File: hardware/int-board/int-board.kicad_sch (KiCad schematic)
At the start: 34 parts, among them J1 PTSM 0,5/4-HH, J2 PTSM 0,5/4-HH, J3 PTSM 0,5/4-HH, J4 PTSM 0,5/4-HH, J5 Pi 40-pin socket, J6 LINK to EXT, J7 PWR link (not fitted), J8 spare ch pads, J9 breakout, U1 LTV-847, U2 LTV-847, U3 LTV-847

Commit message: hardware: INT link headers move into the housing's right-hand slot; review checklist in docs
The enclosure leaves no clearance around the board except the opening for
the four top-edge plugs and a slot on the right-hand side, rows 9-23, the
height of a PTSM socket (David, 2026-09-12). J6 and J7 sit in that slot
with their entries facing the edge, pin row 6.3 mm inside it so the pads
clear the rib's bulges at x 49.8; the MOV position, test points and J8
move to the bottom-left field the links vacated. Header pin 1 stays open
on the board like the spare grounds: the column blocks a track from pin 1
to pin 17, and the router otherwise reached the link from pin 1 and left
17's breakout stranded. A via keepout ring 0.8 mm inside the outline stops
the router placing vias against the 0.3 mm edge rule, which the DSN does
not carry. gen-boards.py also gains the GND_BUS_X import it lost when the
constants moved to gen_tables.py.

Routed, DRC clean, schematic parity kept; Gerbers re-exported. The
"before you order" checklist is docs/rpi-io-boards-review.md.

Co-Authored-By: Claude Fable 5.1 <noreply@anthropic.com>
Claude-Session: https://claude.ai/code/session_01WPMStupqhasFMcGr3goMno
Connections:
- net 3V3: no longer J5.1 (Pin_1)
- no-connect marks 11 -> 12

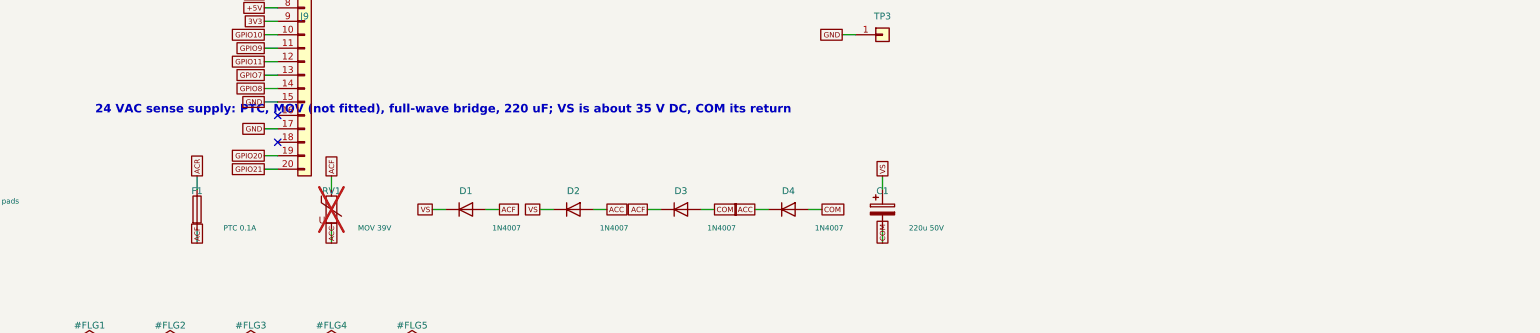
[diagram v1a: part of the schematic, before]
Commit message: hardware: every INT component-side part held to the DIP-socket height; the Pi mapped under the board
The cover's inner depth is unmeasured, but the built board proves it clears
a DIP socket with its chip, about 8 mm, so no fitted part may stand taller.
The 12.5 mm radial capacitor becomes a 100 uF 63 V axial lying flat along
the bottom-left field (6.5 x 18, 6.9 mm); 100 uF holds the 35 V rail's
ripple to 2.8 V at 34 mA and the value is not critical. The PTC disc and the
MOV position lie flat on new pivac footprints. The test points, spare pads
and proto field move to suit.

Appendix A.3 of the plan maps the Pi 4B's connectors onto the INT board
from the RP-008343 mechanical drawing, with the room each leaves on the
solder side at the 16 mm socket stack: none under the USB stacks, where
every joint is trimmed flush, as the built board already requires.

Routed, DRC clean, schematic parity kept; Gerbers re-exported.

Co-Authored-By: Claude Fable 5.1 <noreply@anthropic.com>
Claude-Session: https://claude.ai/code/session_01WPMStupqhasFMcGr3goMno
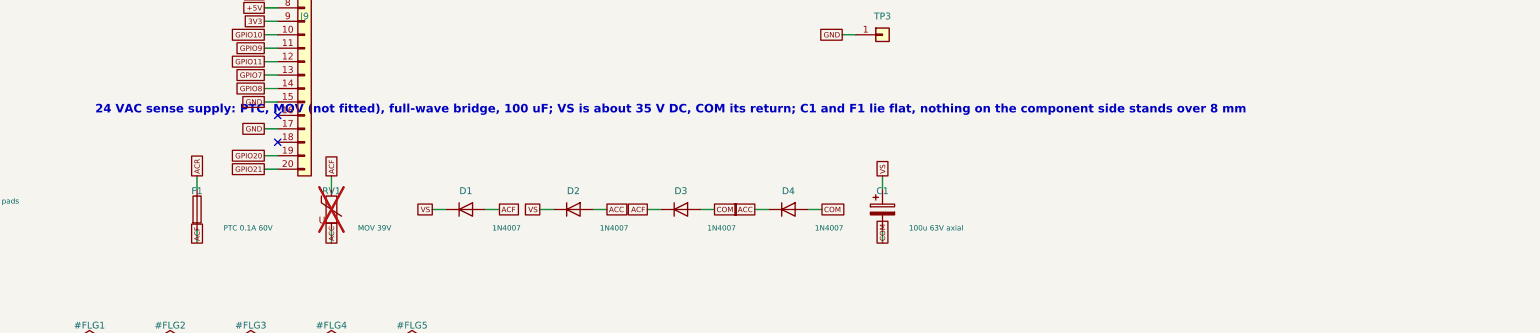
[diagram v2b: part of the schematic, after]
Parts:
- C1: value 220u 50V -> 100u 63V axial; footprint Capacitor_THT:CP_Radial_D10.0mm_P5.00mm -> Capacitor_THT:CP_Axial_L18.0mm_D6.5mm_P25.00mm_Horizontal
- F1: value PTC 0.1A -> PTC 0.1A 60V; footprint pivac:PTC_Radial_P5.08 -> pivac:PTC_Radial_P5.08_Flat
- RV1: footprint pivac:MOV_Radial_P5.0 -> pivac:MOV_Radial_P5.0_Flat
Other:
- note added: "24 VAC sense supply: PTC, MOV (not fitted), full-wave bridge, 100 uF; VS is about 35 V DC, COM its return; C1 and F1 lie flat, nothing on the component side stands over 8 mm"
- note removed: "24 VAC sense supply: PTC, MOV (not fitted), full-wave bridge, 220 uF; VS is about 35 V DC, COM its return"

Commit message: hardware: no through-hole part over the Pi's USB stacks; the capacitor stands between J4 and J6
The USB shells are Pi ground and the rectifier's nets are 35 V above COM,
so a pin tail under a USB stack, where the 16 mm socket stack leaves no
room, is a short waiting to happen (David, 2026-09-12). The bottom-left
field now carries nothing: the capacitor stands between J4 and the link
slot, right of the resistor columns (pitch 3.3 mm) and left of the housing
rib, with the PTC and the MOV position lying flat beside it; the four
diodes form one column at the bottom right past the USB stacks, with the
test points and the spare-channel pads (now a row) below them; the
prototyping field is gone. The link headers' pin row moves to 6.0 mm inside
the edge so their courtyards clear the capacitor's.

docs/rpi-io-boards-review.md and the review page gain a table of what
every reference designator on each board is for.

Routed, DRC clean, schematic parity kept; Gerbers re-exported.

Co-Authored-By: Claude Fable 5.1 <noreply@anthropic.com>
Claude-Session: https://claude.ai/code/session_01WPMStupqhasFMcGr3goMno
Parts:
- J8: footprint pivac:Pads_1x3 -> pivac:Pads_3x1

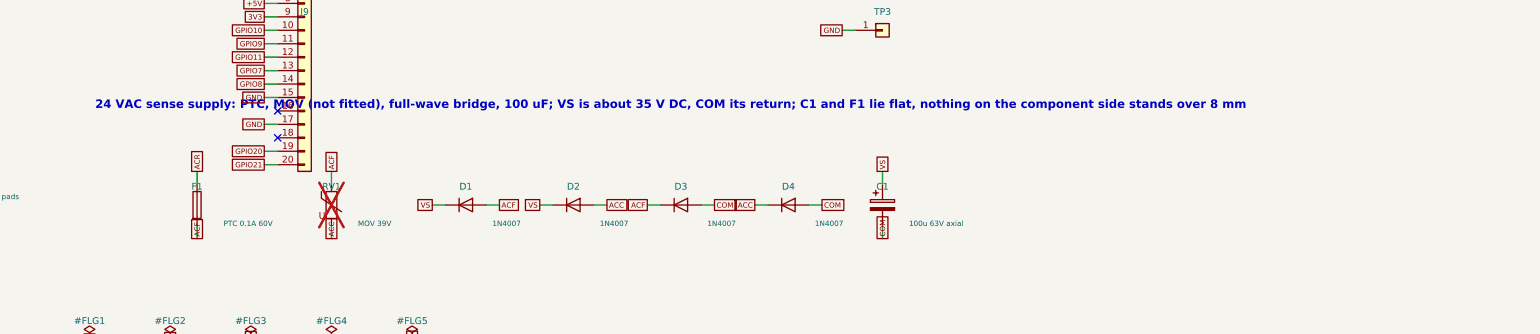
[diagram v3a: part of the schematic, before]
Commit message: hardware: silkscreen tidied, MOV position dropped, copper plots for the review
Plug designators sit below their pin labels (J4's beside the capacitor),
the resistor references run along their bodies, the diode references sit
at the board edge end of each diode, the link header references sit on the
rib strip beside them, the capacitor's beside its lower pad, and the empty
bottom field says why it is empty. The MOV position is gone: the strip
beside the capacitor holds the PTC and the J4 labels, and a clamp on a
class 2 transformer's 24 VAC is a nicety. GPIO8's run from header pin 24
to its breakout pad, which threads the column twice through 0.84 mm gaps,
is laid by hand because the router managed it only sometimes. EXT: C1's
reference moves below the part, clear of the H2 label.

Both boards carry front and back copper plots (back mirrored) from
kicad-cli for checking traces; the review document shows both faces of
each board and the copper.

Co-Authored-By: Claude Fable 5.1 <noreply@anthropic.com>
Claude-Session: https://claude.ai/code/session_01WPMStupqhasFMcGr3goMno
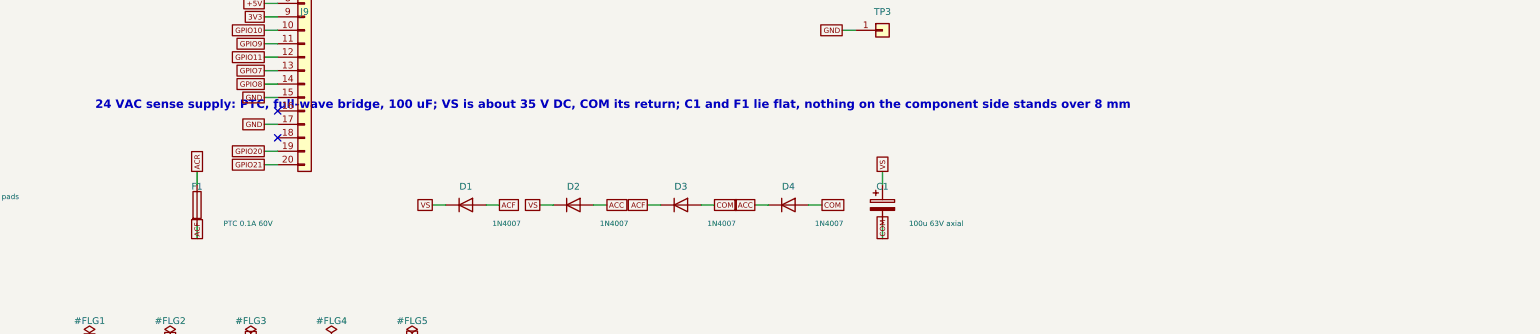
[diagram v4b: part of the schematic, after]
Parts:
- removed RV1: MOV 39V, pivac:MOV_Radial_P5.0_Flat, symbol Device:Varistor
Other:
- note added: "24 VAC sense supply: PTC, full-wave bridge, 100 uF; VS is about 35 V DC, COM its return; C1 and F1 lie flat, nothing on the component side stands over 8 mm"
- note removed: "24 VAC sense supply: PTC, MOV (not fitted), full-wave bridge, 100 uF; VS is about 35 V DC, COM its return; C1 and F1 lie flat, nothing on the component side stands over 8 mm"

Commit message: Rev B boards generated: KiCad, schematics, BOMs and OSH Park gerbers for INT and EXT
gen-boards.py now builds rev B. INT loses the bridge, F1, C1, J7 and J8,
J4 carries HPCOOL, DHWX and SP-E, the sockets sit at x 13 with the resistor
columns on 4.0 mm (the most the housing bulges' rule areas allow), J6 is the
JST GH side-entry header at the slot with VS and COM on pins 6 and 7, and the
DL title block is centred in the bottom field. EXT keeps the probe sockets,
puts the I2C parts in one row under them, and carries the power section:
J3 24 VAC entry at the bottom edge with the sockets' 1.7 mm overhang, F1
standing, D1-D4 at 3.5 mm rows, C3 standing, U3 on a new SIP-8 footprint,
C4, J4 (XH) for the USB-C pigtail, a tie-slot pair, a 6 x 4 proto field and
the GH top-entry link header low at the opening, pin 1 at the bottom on both
boards. Freerouting is not deterministic, so build.sh regenerates and reroutes
each board until DRC is clean and everything is connected; five connections
it kept leaving open are laid as fixed tracks. Both boards are DRC-clean with
nothing unconnected; build.sh now also exports the gerbers and drill files
and zips them.

The plan carries the generated numbers and the state of the build; the layout
SVG matches it.

Co-Authored-By: Claude Fable 5.1 <noreply@anthropic.com>
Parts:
- removed C1: 100u 63V axial, Capacitor_THT:CP_Axial_L18.0mm_D6.5mm_P25.00mm_Horizontal, symbol Device:C_Polarized
- removed D1, D2, D3, D4: 1N4007, Diode_THT:D_DO-41_SOD81_P10.16mm_Horizontal, symbol Device:D
- removed F1: PTC 0.1A 60V, pivac:PTC_Radial_P5.08_Flat, symbol Device:Fuse
- removed J6: LINK to EXT, pivac:PTSM_0.5_5-HH-2.5-THR, symbol Connector_Generic:Conn_01x05
- removed J7: PWR link (not fitted), pivac:PTSM_0.5_4-HH-2.5-THR, symbol Connector_Generic:Conn_01x04
- removed J8: spare ch pads, pivac:Pads_3x1, symbol Connector_Generic:Conn_01x03
- added J6: GH link to EXT, Connector_JST:JST_GH_SM07B-GHS-TB_1x07-1MP_P1.25mm_Horizontal, symbol Connector_Generic:Conn_01x07
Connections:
- net S_SP-C is gone; now on net S_DHWX: R11.2
- net 3V3: now also J6.1 (Pin_1)
- net COM: now also J6.7 (Pin_7)
- net GND: now also J6.5 (Pin_5)
- net GPIO13: now also U3.14 (C2); no longer U3.12 (C3)
- net GPIO19: now also U3.12 (C3); no longer U3.14 (C2)
- net GPIO4: now also J6.4 (Pin_4)
- net SCL: now also J6.3 (Pin_3)
- net SDA: now also J6.2 (Pin_2)
- net S_SP-E: now also J4.3 (Pin_3)
- net VS: now also J6.6 (Pin_6)
- net ACC renamed S_DHWX
- net ACR renamed S_HPCOOL
- net S_HPCOOL: now also R10.2
- removed net S_SP-D: J4.3 (Pin_3), R10.2
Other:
- note added: "Field plugs, PTSM 0,5/4-HH-2,5-THR; position 4 is COM on every plug; twelve channels on twelve positions"
- note added: "J4.1 > G13 (p33)"
- note added: "J4.2 > G19 (p35)"
- note added: "J4.3 > G16 (p36)"
- note added: "Shadow column J9: one pad per header row (rows 1, 2, 16, 18 empty); pins 2 and 4 (5 V) carry nothing, the Pi is fed by USB-C"
- note added: "The sense supply (VS about 35 V DC, COM its return) is made on the EXT board and arrives on J6.6/J6.7."
- note added: "ch10 HPCOOL"
- note added: "ch11 DHWX"
- note added: "pivac INT board rev B: relay-sense inputs on LTV-847 optocouplers; VS/COM arrive from the EXT board"
- note removed: "24 VAC sense supply: PTC, full-wave bridge, 100 uF; VS is about 35 V DC, COM its return; C1 and F1 lie flat, nothing on the component side stands over 8 mm"
- note removed: "Field plugs, PTSM 0,5/4-HH-2,5-THR; position 4 is COM on every plug; J4.1/J4.2 take the 24 VAC"
- note removed: "J4.3 > G19 (p35)"
- note removed: "J8 > G13 (p33)"
- note removed: "J8 > G16 (p36)"
- note removed: "Shadow column J9: one pad per header row (rows 1, 2, 16, 18 empty)"
- note removed: "ch10 SP-D"
- note removed: "ch11 SP-C"
- note removed: "pivac INT board rev A: relay-sense inputs on LTV-847 optocouplers, 24 VAC sense supply"
